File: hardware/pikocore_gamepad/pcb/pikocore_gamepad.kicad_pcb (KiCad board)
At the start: 4 copper layers, 90 x 130 mm, 62 parts, among them J1 PinHeader_1x04_P2.54mm_Vertic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, J4 LCD_ST7789_240x240_7P, J5 JST_PH_B2B-PH-K_1x02_P2.00mm_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, SW1 SW-TH_4P-L4.5-W4.5-P3.00-LS5.5, SW10 SW_Tactile_SPST_Angled_PTS645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, SW11 SW-TH_4P-L4.5-W4.5-P3.00-LS5.5, SW12 SW-TH_4P-L4.5-W4.5-P3.00-LS5.5, SW15 SW-TH_SK12D07VG3, SW2 SW-TH_4P-L4.5-W4.5-P3.00-LS5.5, SW3 SW-TH_4P-L4.5-W4.5-P3.00-LS5.5, SW4 SW-TH_4P-L4.5-W4.5-P3.00-LS5.5, SW5 SW-TH_4P-L4.5-W4.5-P3.00-LS5.5, SW6 SW-TH_4P-L4.5-W4.5-P3.00-LS5.5, SW7 SW-TH_4P-L4.5-W4.5-P3.00-LS5.5, SW8 SW-TH_4P-L4.5-W4.5-P3.00-LS5.5, SW9 SW_Tactile_SPST_Angled_PTS645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, U1 RP2350-Plus_Socket, U2 SOT-23-6, U3 SOIC-8_3.9x4.9mm_P1.27mm, U4 MSOP-8_L3.0-W3.0-P0.65-LS5.0-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, U5 TSSOP-20_L6.5-W4.4-P0.65-LS6.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

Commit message: hw: pikocore_gamepad schematic/PCB regenerated — NAV5 + speaker reloc, checks green
Co-Authored-By: Claude Sonnet 5 <noreply@anthropic.com>
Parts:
- removed SW1, SW2, SW3, SW4: SW-TH_4P-L4.5-W4.5-P3.00-LS5.5, SW-TH_4P-L4.5-W4.5-P3.00-LS5.5
- added SW13: SW-TH_WS-1004-ARL10026, SW-TH_WS-1004-ARL10026, F.Cu at (22.5, 83.0)
- moved J5 94.2 mm to (18.0, 30.0)
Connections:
- U1 pad 31: EXP_GP26 -> BTN_OK
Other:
- board size 90 x 130 mm -> 90 x 105 mm

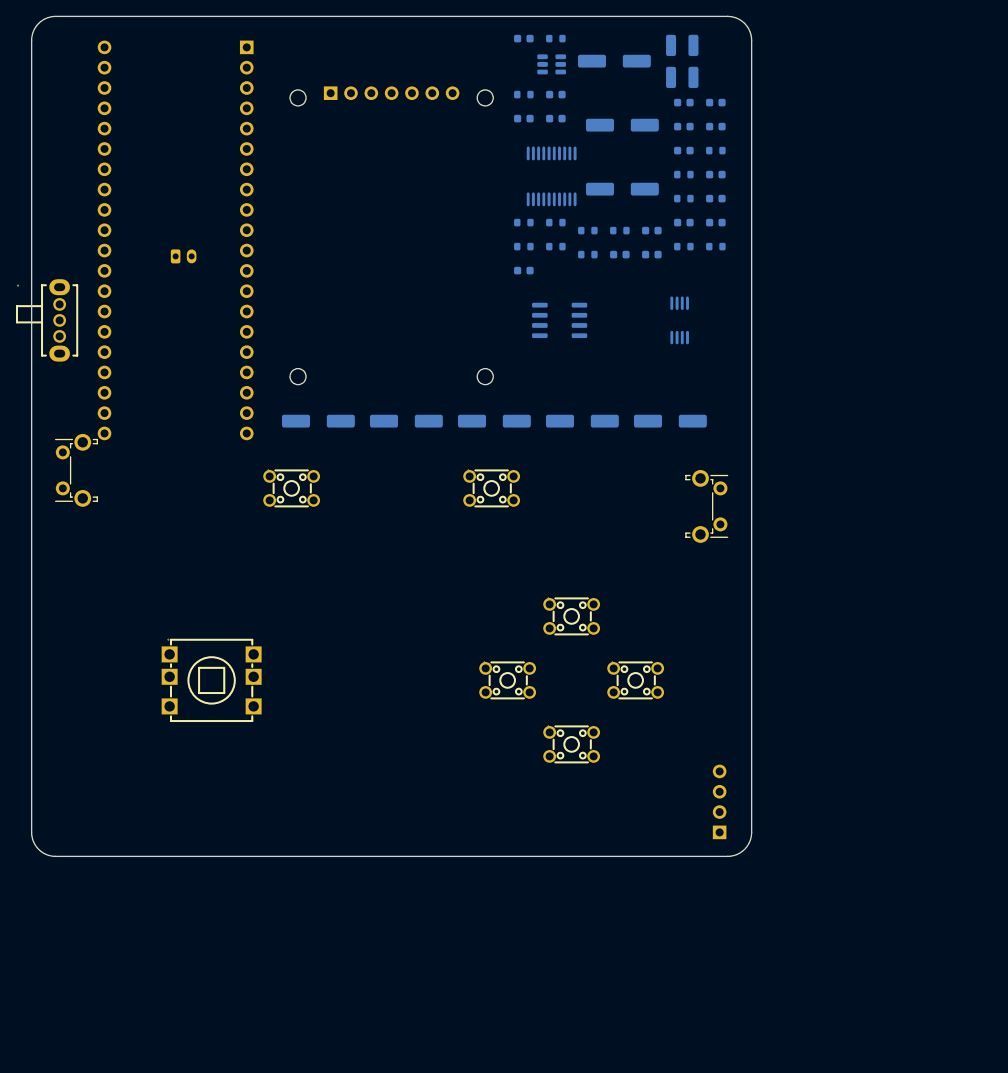
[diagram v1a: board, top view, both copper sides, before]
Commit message: hw: snapshot del pipeline de pikocore_gamepad — punto de rollback
Commit de resguardo, no un cambio con una idea sola. Junta todo el trabajo del
pipeline de PCB que estaba sin commitear, para que exista un estado al que
volver antes de correr el ciclo de ruteo completo, que reescribe el
esquematico, las 5 hojas, el netlist y la placa, y cuyo autorouter no es
determinista.

Sin esto, un `git checkout` despues de un re-ruteo fallido devolvia el
esquematico PLANO de hace dias, no el jerarquico de ahora.

Lo mas importante que entra: tres scripts que el ciclo NECESITA y que estaban
sin trackear —

  plane_vias.py    vias que conectan pads SMD de GND/3V3 a los planos internos
  manual_tracks.py pistas trazadas a mano que entran al DSN como preexistentes
  gen_fab.py       paquete de fabricacion para JLCPCB, con G-0 como puerta

Los dos primeros van ANTES del export al DSN, no despues; el motivo y lo que
costo descubrirlo estan documentados en la checklist.

Y el esquematico partido en 5 hojas jerarquicas, que vivia solo en el working
tree: el root perdio 2993 lineas porque el contenido se mudo a
01_alimentacion, 02_mcu_controles, 03_dac, 04_opamp y 05_salidas, ninguna de
las cuales estaba trackeada. gen_sch.py las genera desde HOJAS.

Estado verificado al momento del commit, corriendo las puertas de verdad:

  201 tests                             OK
  checks/run_all.py (G-0/G-5/G-4/G-2/P) todas pasan
  ERC                                   0 errores, 2 avisos
  DRC                                   2 errores, 7 avisos
  unconnected_items                     0

Los 2 errores de DRC son conocidos y quedan abiertos a proposito: vias de GND
y 3V3 encimadas sobre pads adyacentes de U5 (TSSOP-20, paso 0.65mm), porque
plane_vias.py dimensiona cada via mirando solo pads y no las vias que el mismo
ya coloco. Arreglarlo obliga al ciclo completo, que es justamente lo que este
commit viene a proteger.

Queda fuera a proposito: freerouting-1.9.0.jar (la checklist dice que no se
vers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
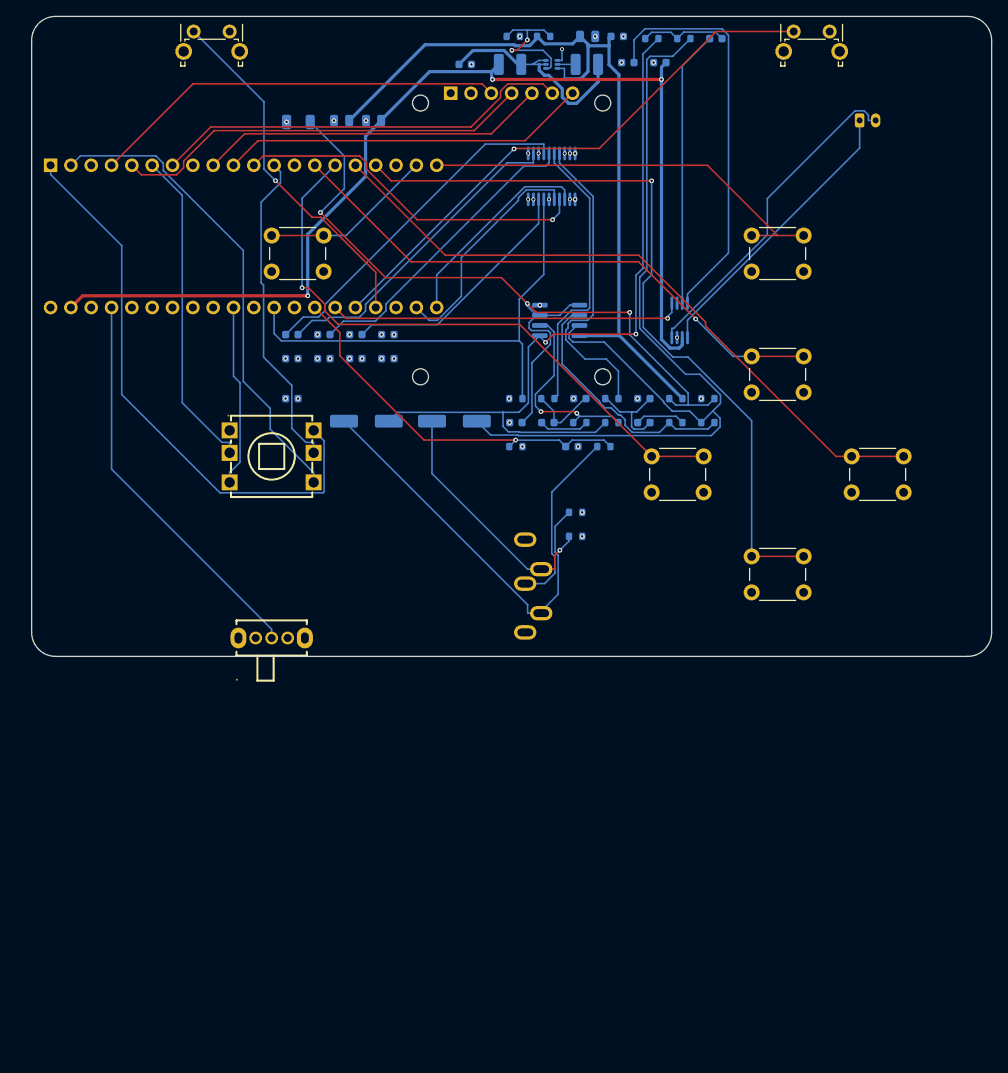
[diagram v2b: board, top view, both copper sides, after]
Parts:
- added C29: C_0603_1608Metric, C_0603_1608Metric, B.Cu at (67.5, 53.8)
- added R18: R_0603_1608Metric, R_0603_1608Metric, B.Cu at (71.5, 53.8)
- added R19: R_0603_1608Metric, R_0603_1608Metric, B.Cu at (68.0, 62.0)
- added R20: R_0603_1608Metric, R_0603_1608Metric, B.Cu at (68.0, 65.0)
- C12, C14, C16: value CP_Elec_6.3x5.4 -> C_0603_1608Metric; footprint CP_Elec_6.3x5.4 -> C_0603_1608Metric
- C19: value CP_Elec_6.3x5.4 -> C_1206_3216Metric; footprint CP_Elec_6.3x5.4 -> C_1206_3216Metric
- C28, C6: value CP_Elec_6.3x5.4 -> C_0805_2012Metric; footprint CP_Elec_6.3x5.4 -> C_0805_2012Metric
- C5: value C_0603_1608Metric -> C_0805_2012Metric; footprint C_0603_1608Metric -> C_0805_2012Metric
- J1: value PinHeader_1x04_P2.54mm_Vertical -> Jack_3.5mm_CUI_SJ1-3535NG_Horizontal; footprint PinHeader_1x04_P2.54mm_Vertical -> Jack_3.5mm_CUI_SJ1-3535NG_Horizontal
- SW11, SW12, SW5, SW6, SW7, SW8: value SW-TH_4P-L4.5-W4.5-P3.00-LS5.5 -> SW_PUSH_6mm; footprint SW-TH_4P-L4.5-W4.5-P3.00-LS5.5 -> SW_PUSH_6mm
- U2: value SOT-23-6 -> SOT-563; footprint SOT-23-6 -> SOT-563
- moved J5 87.2 mm to (103.5, 13.0)
- moved C8 60.4 mm to (32.5, 39.8)
- moved C19 59.7 mm to (33.3, 13.2)
- moved SW9 59.4 mm to (20.2, 1.89), turned to 0 degrees
- moved SW10 57.8 mm to (95.2, 1.89), turned to 0 degrees
- moved C13 56.9 mm to (36.5, 42.8)
- moved C23 54.6 mm to (41.8, 50.6)
- moved SW15 47.7 mm to (30.0, 77.7), turned to 0 degrees
- moved SW12 45.3 mm to (90.0, 27.4)
- moved C15 45.2 mm to (44.5, 42.8)
- moved C11 45.2 mm to (44.5, 39.8)
- moved C24 42.5 mm to (52.8, 50.6)
- moved R6 39.8 mm to (60.5, 47.8)
- moved SW5 39.5 mm to (90.0, 42.5)
- moved SW7 38.9 mm to (102.5, 55.0)
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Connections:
- SW11 pad 2: unconnected-(SW11-A-Pad2) -> GND
- SW12 pad 2: unconnected-(SW12-A-Pad2) -> GND
- SW5 pad 2: unconnected-(SW5-A-Pad2) -> GND
- SW6 pad 2: unconnected-(SW6-A-Pad2) -> GND
- SW7 pad 2: unconnected-(SW7-A-Pad2) -> GND
- SW8 pad 2: unconnected-(SW8-A-Pad2) -> GND
- U2 pad 1: VSYS_F -> BOOST_FB
- U2 pad 2: GND -> VSYS_F
- U2 pad 4: BOOST_FB -> GND
- U2 pad 5: 5V -> BOOST_SW
- U2 pad 6: BOOST_SW -> 5V
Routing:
- net VSYS: track 0.00 -> 134.7 mm, vias 0 -> 3
- net AUDIO_R: track 0.00 -> 115.8 mm
- net VREF25: track 0.00 -> 104.5 mm, vias 0 -> 3
- net 5V: track 0.00 -> 101.3 mm
- net BTN_B: track 0.00 -> 95.9 mm, vias 0 -> 1
- net AUDIO_L: track 0.00 -> 93.7 mm, vias 0 -> 2
- net BTN_A: track 0.00 -> 83.9 mm
- net BTN_Y: track 0.00 -> 76.5 mm, vias 0 -> 1
- net BTN_X: track 0.00 -> 71.0 mm, vias 0 -> 1
- net DPAD_UP: track 0.00 -> 71.0 mm
- net BTN_R: track 0.00 -> 69.1 mm, vias 0 -> 1
- net DAC_XSMT: track 0.00 -> 60.6 mm
- net DPAD_DOWN: track 0.00 -> 60.1 mm
- net BTN_SELECT: track 0.00 -> 52.8 mm
- net LCD_MOSI: track 0.00 -> 52.7 mm
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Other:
- board size 90 x 105 mm -> 120 x 80 mm

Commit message: hw: plane_vias.py — contar vias al dimensionar, y fanout cuando no entra
Cierra los 2 errores de clearance que quedaban y el pad que no ruteaba.

CAUSA. hueco_libre() solo miraba pads de otra net. Las vias que el propio
script iba colocando no entraban en la cuenta, asi que dos pads adyacentes de
nets distintas recibian cada uno su via de 0.5mm sin enterarse el uno del
otro: a 0.65mm de paso quedaban a 0.150mm contra los 0.2mm de la netclass.
Paso en U5 (TSSOP-20), pads 8/9 y 19/20, GND contra 3V3.

Contar las vias arregla el clearance pero deja 3 pads sin via — U5.9, U5.20 y
U2.4, este ultimo tapado hasta ahora por la regla DRC rota de U2. Rendirse
"funciona" porque freerouting suele llevarlos al plano por pista, pero suele:
sobre las MISMAS entradas dio 503 pistas una corrida y 477 la siguiente, y con
U5.20 no le salio dos veces seguidas. Un pad que llega al plano porque al
autorouter le salio es una placa que anda de casualidad.

FANOUT. Cuando no entra en el centro del pad, la via se desplaza a un punto
libre cercano y un tramo corto la une. Tres cosas que costaron una corrida
cada una y estan documentadas en el codigo:

  - pad.GetLayer() devuelve F.Cu en un footprint volteado aunque el unico
    cobre del pad este en B.Cu. Los tres tramos salieron en la cara
    equivocada: cobre huerfano, track_dangling, y la conexion la volvia a
    hacer freerouting. GetLayerSet().CuStack() si dice la verdad.

  - el ancho del tramo no puede ser fijo. La pista arranca en el centro del
    pad y ahi su punta se expande media anchura en TODAS las direcciones,
    tambien hacia el vecino que dejo sin lugar a la via. El tramo de U2.4
    salia en direccion contraria al pad 5 y lo violaba igual, con 0.125mm
    reales = 0.325 de hueco menos 0.200 de radio. Ahora el ancho se achica a
    lo que el hueco permita (0.25mm en U2.4), con piso en 0.2mm.

  - entre las direcciones que entran gana la MAS HOLGADA, no la primera.
    Cumplir el margen no alcanza: la via tambien es un obsta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
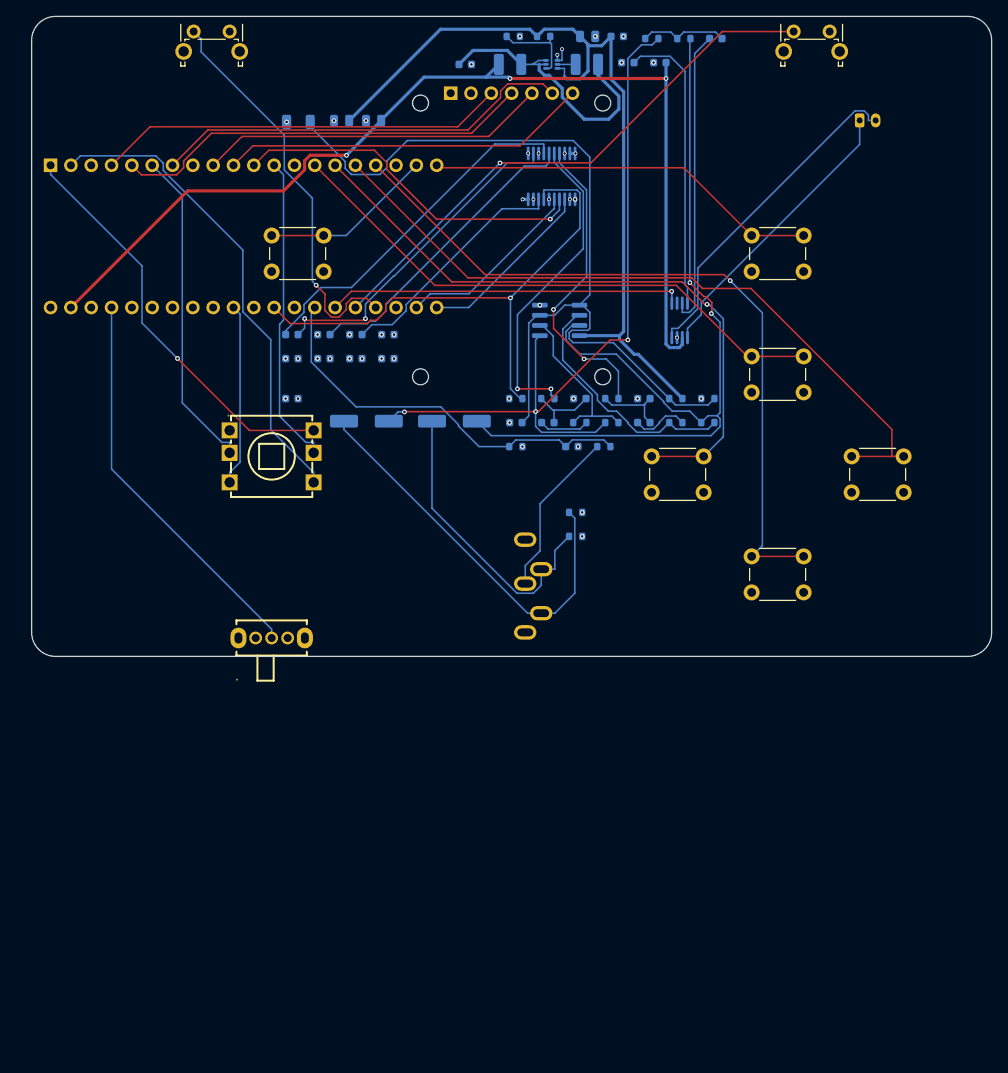
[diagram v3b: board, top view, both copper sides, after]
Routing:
- net DPAD_UP: track 71.0 -> 51.5 mm, vias 0 -> 1
- net SPK_INN: track 51.2 -> 36.6 mm
- net DAC_XSMT: track 60.6 -> 68.1 mm, vias 0 -> 1
- net VSYS_F: track 27.8 -> 35.2 mm
- net VSYS: track 134.7 -> 127.8 mm
- net AUDIO_R: track 115.8 -> 108.9 mm, vias 0 -> 2
- net BTN_A: track 83.9 -> 90.6 mm
- net BOOST_FB: track 16.9 -> 10.4 mm, vias 2 -> 0
- net JACK_R: track 31.7 -> 37.9 mm, vias 1 -> 0
- net BTN_L: track 44.6 -> 50.3 mm
- net I2S_LRCK: track 28.9 -> 23.5 mm
- net VREF25: track 104.5 -> 109.8 mm, vias 3 -> 0
- net BTN_Y: track 76.5 -> 81.2 mm
- net DACOUT_L: track 35.5 -> 40.0 mm, vias 0 -> 2
- net OPL_N: track 24.7 -> 20.6 mm, vias 2 -> 0
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
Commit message: hw: paquete de fabricación con las 4 capas, paridad esquemático↔PCB en 0
gen_fab.py pedía las capas internas por su nombre de usuario (GND/PWR);
kicad-cli 9.0.1 las rechazaba con un aviso y exit 0, y el zip salía con
dos capas de cobre para una placa de cuatro. Ahora usa In1.Cu/In2.Cu y
aborta si falta cualquier gerber obligatorio. También busca kicad-cli en
Program Files, que es donde está en esta máquina.

gen_pcb.py dejaba el FPID sin librería y el Value con el nombre del
footprint: 128 avisos footprint_symbol_mismatch en el DRC con
--schematic-parity. identidad_desde_netlist() los pone desde netlist.py
y finish_pcb.py lo repite al final del ciclo, así la placa ya ruteada
quedó corregida sin re-rutear. C23/C24 (soldadura manual) van DNP
también en el esquemático.

Estado tras la corrida completa de pcb-verify: 201 tests, G-0/G-5/G-4/
G-2/placement OK, ERC 0 errores, DRC 0 errores / 0 nets sin rutear /
0 paridad. README de hardware y checklist JLCPCB actualizados.

Co-Authored-By: Claude Fable 5.1 <noreply@anthropic.com>
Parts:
- C10, C11, C13, C15, C20, C27, C7: value C_0603_1608Metric -> 100nF; footprint C_0603_1608Metric -> Capacitor_SMD:C_0603_1608Metric
- C12, C14, C16, C29, C4: value C_0603_1608Metric -> 10uF; footprint C_0603_1608Metric -> Capacitor_SMD:C_0603_1608Metric
- C17, C18: value C_0603_1608Metric -> 2.2nF; footprint C_0603_1608Metric -> Capacitor_SMD:C_0603_1608Metric
- C19: value C_1206_3216Metric -> 100uF; footprint C_1206_3216Metric -> Capacitor_SMD:C_1206_3216Metric
- C21, C22, C25, C26: value C_0603_1608Metric -> 1uF; footprint C_0603_1608Metric -> Capacitor_SMD:C_0603_1608Metric
- C23, C24: value CP_Elec_6.3x5.4 -> 470uF; footprint CP_Elec_6.3x5.4 -> Capacitor_SMD:CP_Elec_6.3x5.4
- C28, C5, C6: value C_0805_2012Metric -> 22uF; footprint C_0805_2012Metric -> Capacitor_SMD:C_0805_2012Metric
- C8, C9: value C_0603_1608Metric -> 2.2uF; footprint C_0603_1608Metric -> Capacitor_SMD:C_0603_1608Metric
- J1: value Jack_3.5mm_CUI_SJ1-3535NG_Horizontal -> PHONES; footprint Jack_3.5mm_CUI_SJ1-3535NG_Horizontal -> Connector_Audio:Jack_3.5mm_CUI_SJ1-3535NG_Horizontal
- J4: value LCD_ST7789_240x240_7P -> ST7789_240x240; footprint LCD_ST7789_240x240_7P -> gamesetup_fp:LCD_ST7789_240x240_7P
- J5: value JST_PH_B2B-PH-K_1x02_P2.00mm_Vertical -> SPEAKER 8R; footprint JST_PH_B2B-PH-K_1x02_P2.00mm_Vertical -> Connector_JST:JST_PH_B2B-PH-K_1x02_P2.00mm_Vertical
- L1, L2: value L_1210_3225Metric -> 2.2uH; footprint L_1210_3225Metric -> Inductor_SMD:L_1210_3225Metric
- R10, R12, R14, R16, R17, R9: value R_0603_1608Metric -> 10k; footprint R_0603_1608Metric -> Resistor_SMD:R_0603_1608Metric
- R11, R13: value R_0603_1608Metric -> 20k; footprint R_0603_1608Metric -> Resistor_SMD:R_0603_1608Metric
- R15: value R_0603_1608Metric -> 47k; footprint R_0603_1608Metric -> Resistor_SMD:R_0603_1608Metric
- R18, R19, R20: value R_0603_1608Metric -> 4.7k; footprint R_0603_1608Metric -> Resistor_SMD:R_0603_1608Metric
- R4: value R_0603_1608Metric -> 200k; footprint R_0603_1608Metric -> Resistor_SMD:R_0603_1608Metric
- R5: value R_0603_1608Metric -> 27k; footprint R_0603_1608Metric -> Resistor_SMD:R_0603_1608Metric
- R6: value R_0603_1608Metric -> 100k; footprint R_0603_1608Metric -> Resistor_SMD:R_0603_1608Metric
- R7, R8: value R_0603_1608Metric -> 470R; footprint R_0603_1608Metric -> Resistor_SMD:R_0603_1608Metric
- SW10: value SW_Tactile_SPST_Angled_PTS645Vx39-2LFS -> BTN_R; footprint SW_Tactile_SPST_Angled_PTS645Vx39-2LFS -> Button_Switch_THT:SW_Tactile_SPST_Angled_PTS645Vx39-2LFS
- SW11: value SW_PUSH_6mm -> BTN_START; footprint SW_PUSH_6mm -> Button_Switch_THT:SW_PUSH_6mm
- SW12: value SW_PUSH_6mm -> BTN_SELECT; footprint SW_PUSH_6mm -> Button_Switch_THT:SW_PUSH_6mm
- SW13: value SW-TH_WS-1004-ARL10026 -> NAV5; footprint SW-TH_WS-1004-ARL10026 -> gamesetup_lcsc:SW-TH_WS-1004-ARL10026
- SW15: value SW-TH_SK12D07VG3 -> PWR; footprint SW-TH_SK12D07VG3 -> gamesetup_lcsc:SW-TH_SK12D07VG3
- SW5: value SW_PUSH_6mm -> BTN_X; footprint SW_PUSH_6mm -> Button_Switch_THT:SW_PUSH_6mm
- SW6: value SW_PUSH_6mm -> BTN_Y; footprint SW_PUSH_6mm -> Button_Switch_THT:SW_PUSH_6mm
- SW7: value SW_PUSH_6mm -> BTN_A; footprint SW_PUSH_6mm -> Button_Switch_THT:SW_PUSH_6mm
- SW8: value SW_PUSH_6mm -> BTN_B; footprint SW_PUSH_6mm -> Button_Switch_THT:SW_PUSH_6mm
- SW9: value SW_Tactile_SPST_Angled_PTS645Vx39-2LFS -> BTN_L; footprint SW_Tactile_SPST_Angled_PTS645Vx39-2LFS -> Button_Switch_THT:SW_Tactile_SPST_Angled_PTS645Vx39-2LFS
- U1: value RP2350-Plus_Socket -> RP2350-Plus-16MB; footprint RP2350-Plus_Socket -> gamesetup_fp:RP2350-Plus_Socket
- U2: value SOT-563 -> TPS61023DRLR; footprint SOT-563 -> Package_TO_SOT_SMD:SOT-563
- U3: value SOIC-8_3.9x4.9mm_P1.27mm -> PT2308-S; footprint SOIC-8_3.9x4.9mm_P1.27mm -> Package_SO:SOIC-8_3.9x4.9mm_P1.27mm
- U4: value MSOP-8_L3.0-W3.0-P0.65-LS5.0-BL -> PAM8302A; footprint MSOP-8_L3.0-W3.0-P0.65-LS5.0-BL -> gamesetup_lcsc:MSOP-8_L3.0-W3.0-P0.65-LS5.0-BL
- U5: value TSSOP-20_L6.5-W4.4-P0.65-LS6.4-BL -> PCM5102APWR; footprint TSSOP-20_L6.5-W4.4-P0.65-LS6.4-BL -> gamesetup_lcsc:TSSOP-20_L6.5-W4.4-P0.65-LS6.4-BL
